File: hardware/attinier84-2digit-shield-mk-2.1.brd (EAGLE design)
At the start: 29 x 31 mm, 10 parts, among them IC1 TMP36, U1 ATTINIER84_SHIELD1551G

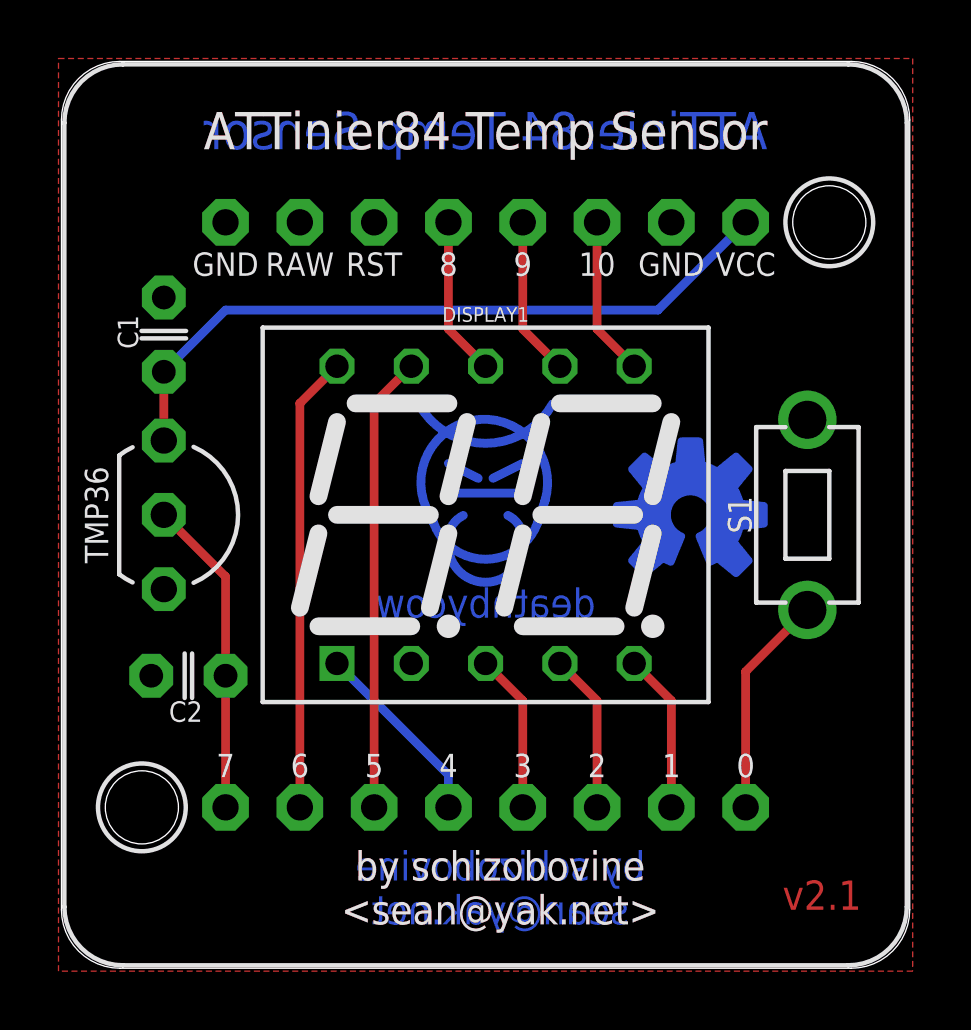
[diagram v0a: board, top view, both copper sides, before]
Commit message: small tweak to capacitor layout
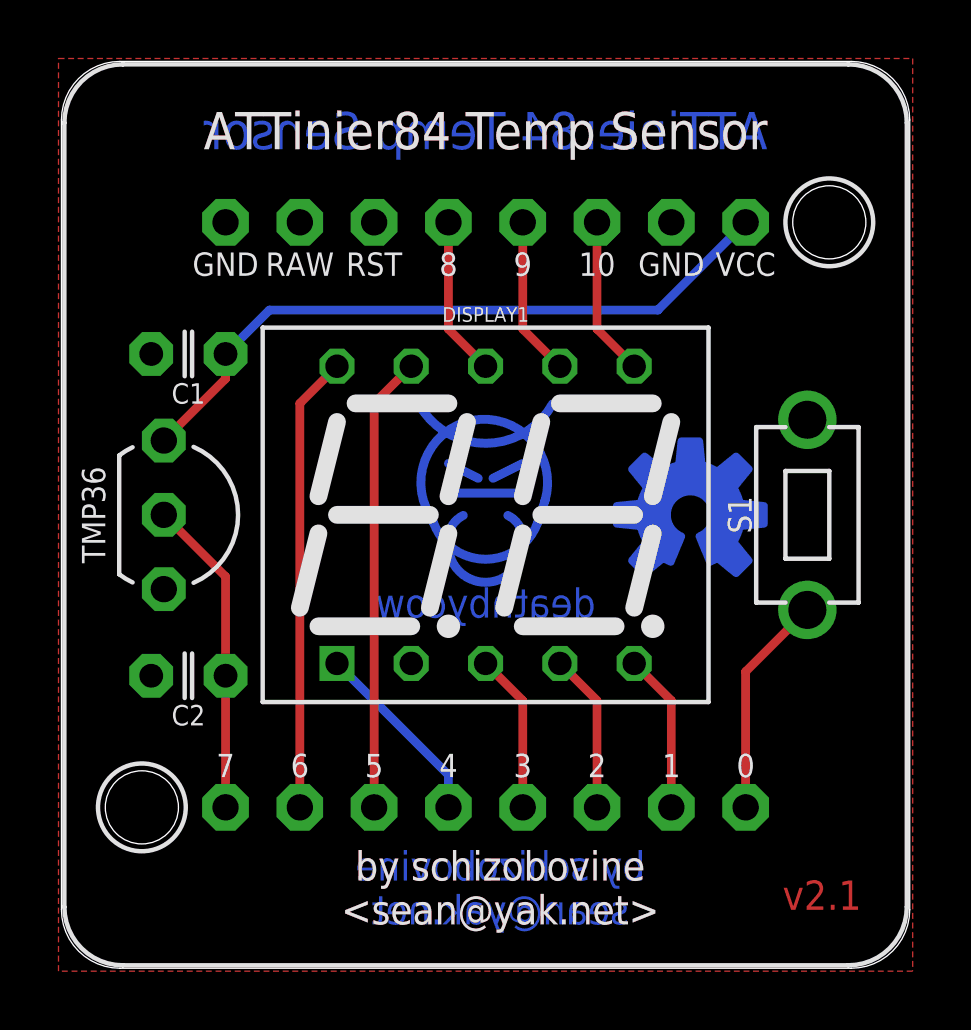
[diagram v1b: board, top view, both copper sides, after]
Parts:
- moved C1 1.07 mm to (4.34, 21.0), turned to 180 degrees
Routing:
- net VCC: track 24.4 -> 23.5 mm
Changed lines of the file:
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@@
 <setting verticaltext="up"/>
 </settings>
-<grid distance="0.25" unitdist="mm" unit="mm" style="lines" multiple="2" display="yes" altdistance="1" altunitdist="mil" altunit="mil"/>
+<grid distance="0.5" unitdist="mm" unit="mm" style="lines" multiple="2" display="yes" altdistance="1" altunitdist="mil" altunit="mil"/>
 <layers>
 <layer number="1" name="Top" color="4" fill="1" visible="yes" active="yes"/>
@@
 <element name="DISPLAY1" library="A_butts" package="7SEG_2DIG_14MM" value="7SEG_2DIG14MM" x="14.5" y="15.5"/>
 <element name="IC1" library="A_butts" package="TO-92-AMMO" value="TMP36" x="3.5" y="15.5" smashed="yes" rot="R270">
-<attribute name="VALUE" x="1.599" y="15.5" size="0.8" layer="21" font="vector" ratio="12" rot="R270" align="top-center"/>
+<attribute name="VALUE" x="1.5" y="15.5" size="0.8" layer="21" font="vector" ratio="12" rot="R270" align="top-center"/>
 </element>
 <element name="U$1" library="A_butts" package="CC-BY-SA-4.0-NO-URL" value="" x="7.5" y="15.5" rot="MR0"/>
 <element name="U$2" library="A_butts" package="COW_SMALL_METAL" value="" x="14.5" y="16.75" rot="MR0"/>
 <element name="U$3" library="A_butts" package="OSHWLOGO_BOT_0.2_A" value="" x="21.5" y="15.5"/>
-<element name="C1" library="A_butts" package="C025-024X044" value="0.1uF" x="3.5" y="21.66" smashed="yes" rot="R90">
-<attribute name="NAME" x="2.624" y="21.75" size="0.7" layer="25" font="vector" ratio="12" rot="R90" align="bottom-center"/>
-<attribute name="VALUE" x="4.446" y="21.75" size="0.7" layer="27" font="vector" ratio="12" rot="R270" align="bottom-center"/>
+<element name="C1" library="A_butts" package="C025-024X044" value="0.1uF" x="4.34" y="21" smashed="yes" rot="R180">
+<attribute name="NAME" x="4.34" y="20" size="0.7" layer="25" font="vector" ratio="12" rot="R180" align="bottom-center"/>
+<attribute name="VALUE" x="4.34" y="22" size="0.7" layer="27" font="vector" ratio="12" align="bottom-center"/>
 </element>
 <element name="C2" library="A_butts" package="C025-024X044" value="0.1uF" x="4.34" y="10" smashed="yes" rot="R180">
-<attribute name="NAME" x="4.25" y="9.124" size="0.7" layer="25" font="vector" ratio="12" rot="R180" align="bottom-center"/>
-<attribute name="VALUE" x="4.25" y="10.946" size="0.7" layer="27" font="vector" ratio="12" align="bottom-center"/>
+<attribute name="NAME" x="4.34" y="9" size="0.7" layer="25" font="vector" ratio="12" rot="R180" align="bottom-center"/>
+<attribute name="VALUE" x="4.34" y="11" size="0.7" layer="27" font="vector" ratio="12" align="bottom-center"/>
 </element>
 <element name="S1" library="A_butts" package="DTS-3-SMALL-PADS" value="SPST-NO-TACT3MM-PTH-SMALL-PADS" x="25.5" y="15.5" rot="R90"/>
@@
 <contactref element="IC1" pad="1"/>
 <wire x1="23.39" y1="25.5" x2="20.39" y2="22.5" width="0.3" layer="16"/>
-<wire x1="20.39" y1="22.5" x2="5.61" y2="22.5" width="0.3" layer="16"/>
-<wire x1="5.61" y1="22.5" x2="3.5" y2="20.39" width="0.3" layer="16"/>
-<wire x1="3.5" y1="18.04" x2="3.5" y2="20.39" width="0.3" layer="1"/>
+<wire x1="20.39" y1="22.5" x2="7.11" y2="22.5" width="0.3" layer="16"/>
+<wire x1="7.11" y1="22.5" x2="5.61" y2="21" width="0.3" layer="16"/>
+<wire x1="5.61" y1="21" x2="5.61" y2="20.15" width="0.3" layer="1"/>
+<wire x1="5.61" y1="20.15" x2="3.5" y2="18.04" width="0.3" layer="1"/>
 </signal>
 <signal name="DIG2">
